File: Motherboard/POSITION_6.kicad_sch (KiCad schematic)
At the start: 27 parts, among them Q24 MOSFET_N_(ZVN3320FTA), Q26 MOSFET_N_(DMN61D8LQ-13)

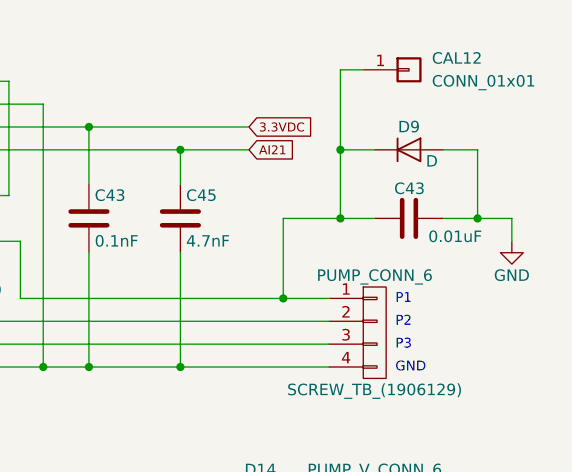
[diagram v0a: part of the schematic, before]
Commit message: Schematic ready.  Going to clean up directory now.
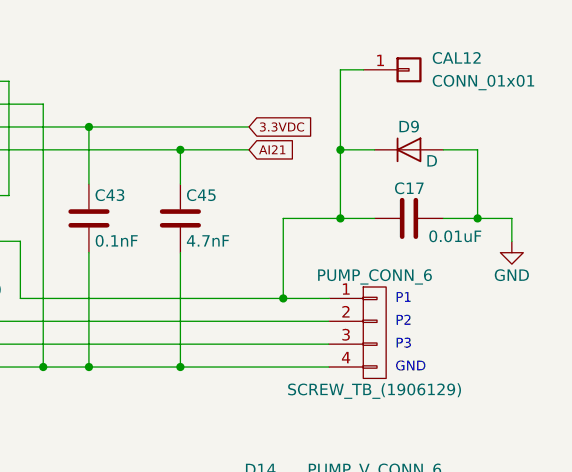
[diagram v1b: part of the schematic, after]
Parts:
- C17: renamed from C43; footprint Capacitors_SMD:C_1206 -> Capacitor_SMD:C_1206_3216Metric
- C43, C44, C45, C46: footprint Capacitors_SMD:C_1206 -> Capacitor_SMD:C_1206_3216Metric
- CAL11, CAL12: footprint (none) -> Smart_Tank:FEMALE_SPADE_QC_(TE_63969-1)
- CTRL_SHUNT_6, PUMP_SHUNT_6: footprint _GARRETTS_PARTS:SHUNT_(WSL40261L000FEA) -> Smart_Tank:SHUNT_(WSL40261L000FEA)
- D14, D9: footprint Diodes_SMD:SOD-123 -> Diode_SMD:D_SMA
- Q24: footprint TO_SOT_Packages_SMD:SOT-23 -> Package_TO_SOT_SMD:SOT-23
- R12, R85, R88, R91, R92, R93: footprint Resistors_SMD:R_1206 -> Resistor_SMD:R_1206_3216Metric
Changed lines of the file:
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@@
 			)
 		)
-		(property "Footprint" ""
+		(property "Footprint" "Smart_Tank:FEMALE_SPADE_QC_(TE_63969-1)"
 			(at 195.58 106.68 0)
 			(effects
@@
 			)
 		)
-		(property "Footprint" ""
+		(property "Footprint" "Smart_Tank:FEMALE_SPADE_QC_(TE_63969-1)"
 			(at 254 31.75 0)
 			(effects
@@
 			)
 		)
-		(property "Footprint" "Resistors_SMD:R_1206"
+		(property "Footprint" "Resistor_SMD:R_1206_3216Metric"
 			(at 74.168 41.91 90)
 			(effects
@@
 			)
 		)
-		(property "Footprint" "Resistors_SMD:R_1206"
+		(property "Footprint" "Resistor_SMD:R_1206_3216Metric"
 			(at 117.348 80.01 90)
 			(effects
@@
 			)
 		)
-		(property "Footprint" "Resistors_SMD:R_1206"
+		(property "Footprint" "Resistor_SMD:R_1206_3216Metric"
 			(at 190.5 76.962 90)
 			(effects
@@
 			)
 		)
-		(property "Footprint" "Resistors_SMD:R_1206"
+		(property "Footprint" "Resistor_SMD:R_1206_3216Metric"
 			(at 94.488 97.79 90)
 			(effects
@@
 			)
 		)
-		(property "Footprint" "_GARRETTS_PARTS:SHUNT_(WSL40261L000FEA)"
+		(property "Footprint" "Smart_Tank:SHUNT_(WSL40261L000FEA)"
 			(at 195.58 138.938 90)
 			(effects
@@
 			)
 		)
-		(property "Footprint" "Capacitors_SMD:C_1206"
+		(property "Footprint" "Capacitor_SMD:C_1206_3216Metric"
 			(at 219.4052 138.43 0)
 			(effects
@@
 			)
 		)
-		(property "Footprint" "Capacitors_SMD:C_1206"
+		(property "Footprint" "Capacitor_SMD:C_1206_3216Metric"
 			(at 229.5652 138.43 0)
 			(effects
@@
 			)
 		)
-		(property "Footprint" "_GARRETTS_PARTS:SHUNT_(WSL40261L000FEA)"
+		(property "Footprint" "Smart_Tank:SHUNT_(WSL40261L000FEA)"
 			(at 195.58 52.578 90)
 			(effects
@@
 			)
 		)
-		(property "Footprint" "Capacitors_SMD:C_1206"
+		(property "Footprint" "Capacitor_SMD:C_1206_3216Metric"
 			(at 219.4052 52.07 0)
 			(effects
@@
 			)
 		)
-		(property "Footprint" "Diodes_SMD:SOD-123"
+		(property "Footprint" "Diode_SMD:D_SMA"
 			(at 254 40.64 0)
 			(effects
@@
 			)
 		)
-		(property "Footprint" "Resistors_SMD:R_1206"
+		(property "Footprint" "Resistor_SMD:R_1206_3216Metric"
 			(at 185.928 85.09 90)
 			(effects
@@
 			)
 		)
-		(property "Footprint" "Capacitors_SMD:C_1206"
+		(property "Footprint" "Capacitor_SMD:C_1206_3216Metric"
 			(at 229.5652 52.07 0)
 			(effects
@@
 			)
 		)
-		(property "Footprint" "Diodes_SMD:SOD-123"
+		(property "Footprint" "Diode_SMD:D_SMA"
 			(at 237.49 78.74 0)
 			(effects
@@
 			)
 		)
-		(property "Footprint" "TO_SOT_Packages_SMD:SOT-23"
+		(property "Footprint" "Package_TO_SOT_SMD:SOT-23"
 			(at 119.38 93.345 0)
 			(effects
@@
 		(on_board yes)
 		(dnp no)
-		(property "Reference" "C43"
+		(property "Reference" "C17"
 			(at 255.778 44.958 90)
 			(effects
@@
 			)
 		)
-		(property "Footprint" "Capacitors_SMD:C_1206"
+		(property "Footprint" "Capacitor_SMD:C_1206_3216Metric"
 			(at 257.81 47.2948 0)
 			(effects
@@
 			(project "Smart Tank Motherboard"
 				(path "/9bd0ace5-d8c1-442c-86d3-58cb44e43f85/00000000-0000-0000-0000-000057a940a2"
-					(reference "C43")
+					(reference "C17")
 					(unit 1)
 				)
@@
 			)
 		)
-		(property "Footprint" "Resistors_SMD:R_1206"
+		(property "Footprint" "Resistor_SMD:R_1206_3216Metric"
 			(at 101.6 90.932 90)
 			(effects

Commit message: Started cleaning out old parts from PCB.
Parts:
- PUMP_V_CONN_6: footprint Smart_Tank:PHNX_TB_SCREW_4_POS_(1729144) -> Smart_Tank:PHX_TB_HDR_4_POS_STR_(1755752)
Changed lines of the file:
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@@
 			)
 		)
-		(property "Footprint" "Smart_Tank:PHNX_TB_SCREW_4_POS_(1729144)"
+		(property "Footprint" "Smart_Tank:PHX_TB_HDR_4_POS_STR_(1755752)"
 			(at 250.19 82.55 0)
 			(effects

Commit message: Almost done with re-routing.
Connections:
- net POS_6_SPARE renamed POS_6_SPR_1
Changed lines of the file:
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@@
 		)
 	)
-	(global_label "POS_6_SPARE"
+	(global_label "POS_6_SPR_1"
 		(shape input)
 		(at 58.42 58.42 0)

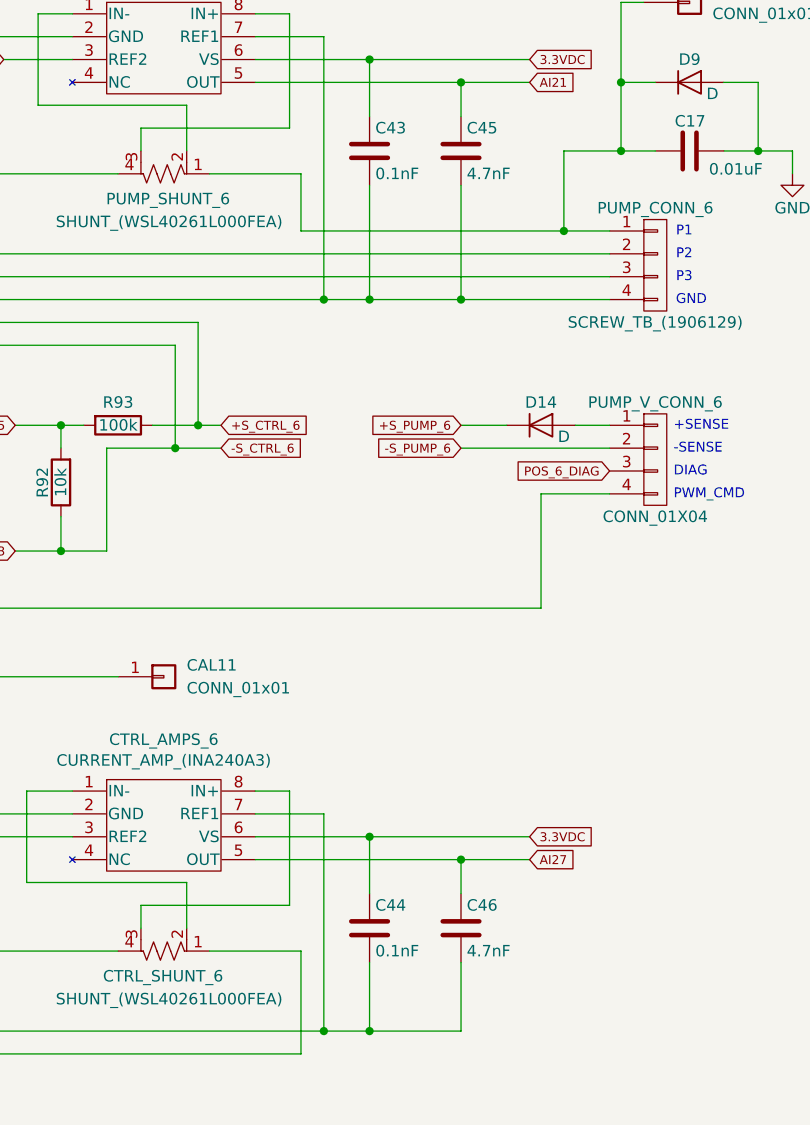
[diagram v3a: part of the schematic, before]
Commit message: Capacitor part issues...
Made these changes...

Concerning C13, C15, C27, C28, C31, C32, C35, C36, C39, C40, C43, C44
The schematic is wrong, and the BOM is correct.  These should all be 0.1uF
Concerning C20, C21, C29, C30, C33, C34, C37, C38, C41, C42, C45, C46
The BOM is wrong, and the schematic is correct.  These should all be 4.7nF
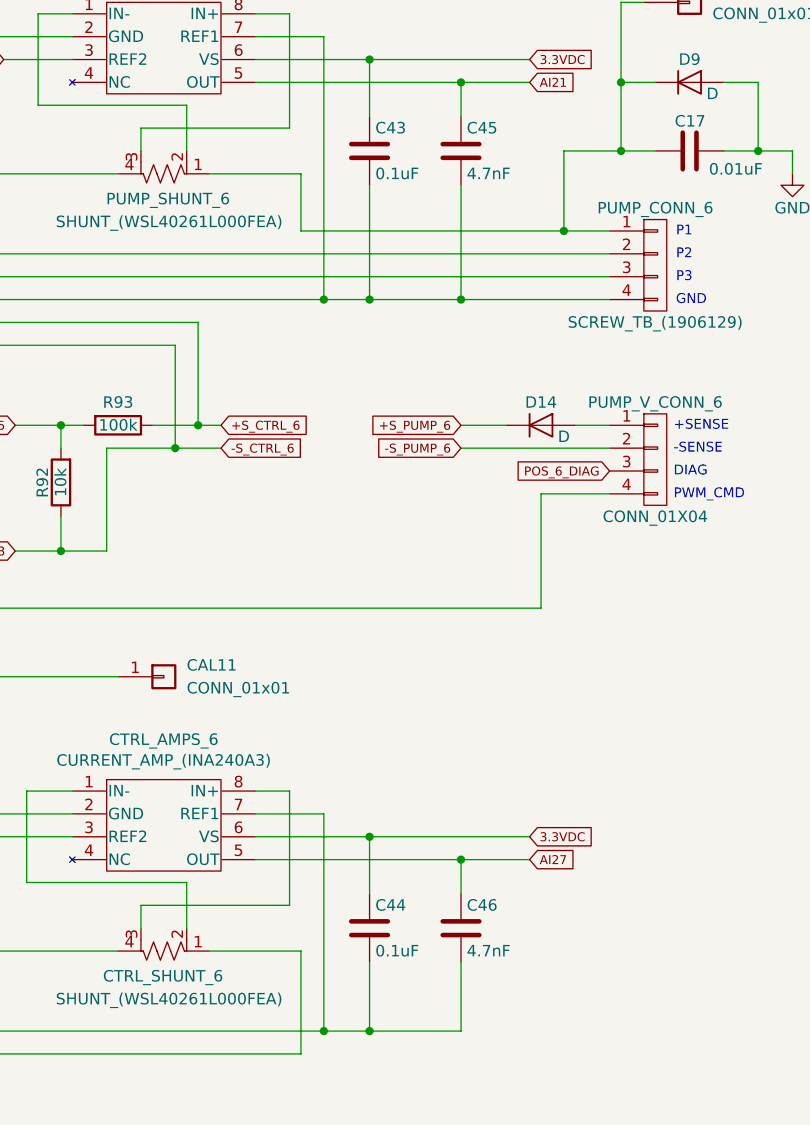
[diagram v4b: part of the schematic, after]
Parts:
- C43, C44: value 0.1nF -> 0.1uF
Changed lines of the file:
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@@
 			)
 		)
-		(property "Value" "0.1nF"
+		(property "Value" "0.1uF"
 			(at 219.075 137.16 0)
 			(effects
@@
 			)
 		)
-		(property "Value" "0.1nF"
+		(property "Value" "0.1uF"
 			(at 219.075 50.8 0)
 			(effects
